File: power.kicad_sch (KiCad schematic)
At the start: 30 parts, among them J1 USB_C_Receptacle_USB2.0_16P, J2 Conn_01x02_MountingPin, Q1 Si2305CDS, Q2 Si2305CDS, Q3 SS8050, SW1 SW_Push, U1 HT7533-1, U2 TP4056-42-ESOP8

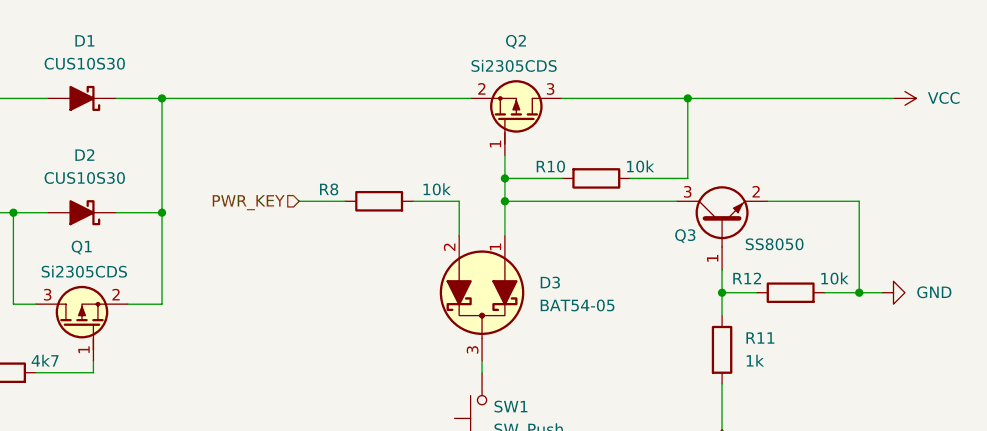
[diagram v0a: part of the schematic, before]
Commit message: 更正电源开关电路的原理错误
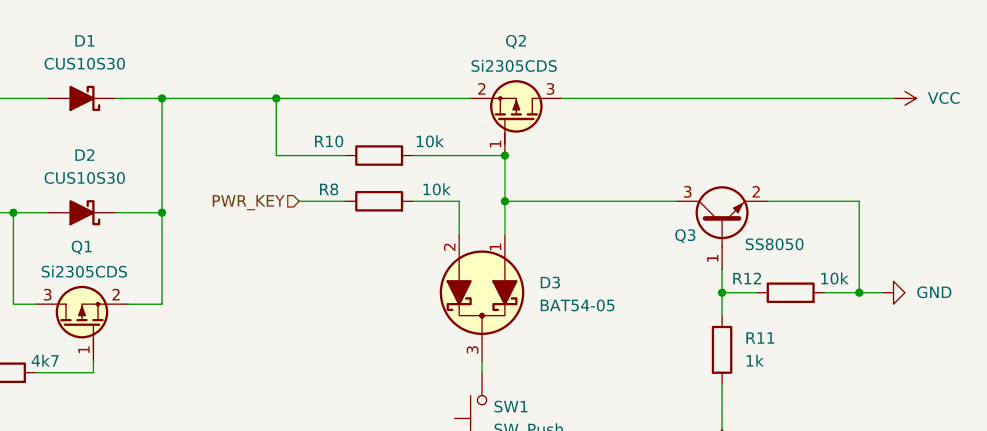
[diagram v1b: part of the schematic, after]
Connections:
- net VCC: no longer R10.1
- net at D1.1 (K), D2.1 (K), Q1.2 (S)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: now also R10.1
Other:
- moved on the sheet: R10
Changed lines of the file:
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@@
+	)
+	(junction
+		(at 203.2 41.91)
+		(diameter 0)
+		(color 0 0 0 0)
 	)
 	(junction
@@
 	)
 	(junction
-		(at 203.2 44.45)
+		(at 177.8 35.56)
 		(diameter 0)
 		(color 0 0 0 0)
@@
 	(junction
 		(at 50.8 118.11)
-		(diameter 0)
-		(color 0 0 0 0)
-	)
-	(junction
-		(at 223.52 35.56)
 		(diameter 0)
 		(color 0 0 0 0)
@@
 	(wire
 		(pts
+			(xy 177.8 35.56) (xy 199.39 35.56)
+		)
+		(stroke
+			(width 0)
+			(type default)
+		)
+	)
+	(wire
+		(pts
+			(xy 177.8 35.56) (xy 177.8 41.91)
+		)
+		(stroke
+			(width 0)
+			(type default)
+		)
+	)
+	(wire
+		(pts
 			(xy 90.17 55.88) (xy 97.79 55.88)
 		)
@@
 	(wire
 		(pts
-			(xy 165.1 35.56) (xy 199.39 35.56)
+			(xy 165.1 35.56) (xy 177.8 35.56)
 		)
 		(stroke
@@
 	(wire
 		(pts
-			(xy 203.2 44.45) (xy 209.55 44.45)
-		)
-		(stroke
-			(width 0)
-			(type default)
-		)
-	)
-	(wire
-		(pts
 			(xy 95.25 35.56) (xy 95.25 48.26)
 		)
@@
 	(wire
 		(pts
-			(xy 223.52 35.56) (xy 246.38 35.56)
-		)
-		(stroke
-			(width 0)
-			(type default)
-		)
-	)
-	(wire
-		(pts
 			(xy 118.11 55.88) (xy 119.38 55.88)
 		)
@@
 	(wire
 		(pts
-			(xy 217.17 44.45) (xy 223.52 44.45)
-		)
-		(stroke
-			(width 0)
-			(type default)
-		)
-	)
-	(wire
-		(pts
 			(xy 165.1 35.56) (xy 165.1 48.26)
 		)
@@
 	(wire
 		(pts
+			(xy 193.04 41.91) (xy 203.2 41.91)
+		)
+		(stroke
+			(width 0)
+			(type default)
+		)
+	)
+	(wire
+		(pts
 			(xy 148.59 58.42) (xy 148.59 48.26)
 		)
@@
 	(wire
 		(pts
-			(xy 209.55 35.56) (xy 223.52 35.56)
+			(xy 209.55 35.56) (xy 246.38 35.56)
 		)
 		(stroke
@@
 	(wire
 		(pts
-			(xy 203.2 46.99) (xy 203.2 44.45)
+			(xy 203.2 41.91) (xy 203.2 46.99)
 		)
 		(stroke
@@
 	(wire
 		(pts
-			(xy 223.52 44.45) (xy 223.52 35.56)
-		)
-		(stroke
-			(width 0)
-			(type default)
-		)
-	)
-	(wire
-		(pts
 			(xy 81.28 114.3) (xy 100.33 114.3)
 		)
@@
 	(wire
 		(pts
-			(xy 203.2 41.91) (xy 203.2 44.45)
-		)
-		(stroke
-			(width 0)
-			(type default)
-		)
-	)
-	(wire
-		(pts
 			(xy 113.03 114.3) (xy 119.38 114.3)
 		)
@@
 		(pts
 			(xy 128.27 48.26) (xy 148.59 48.26)
+		)
+		(stroke
+			(width 0)
+			(type default)
+		)
+	)
+	(wire
+		(pts
+			(xy 185.42 41.91) (xy 177.8 41.91)
 		)
 		(stroke
@@
 	(symbol
 		(lib_id "Device:R")
-		(at 213.36 44.45 270)
+		(at 189.23 41.91 90)
 		(unit 1)
 		(exclude_from_sim no)
@@
 		(dnp no)
 		(property "Reference" "R10"
-			(at 208.28 43.18 90)
+			(at 183.642 40.386 90)
 			(effects
 				(font
@@
 		)
 		(property "Value" "10k"
-			(at 218.186 43.18 90)
+			(at 194.818 40.386 90)
 			(effects
 				(font
@@
 		)
 		(property "Footprint" "Resistor_SMD:R_0603_1608Metric"
-			(at 213.36 42.672 90)
+			(at 189.23 43.688 90)
 			(effects
 				(font
@@
 		)
 		(property "Datasheet" "~"
-			(at 213.36 44.45 0)
+			(at 189.23 41.91 0)
 			(effects
 				(font
@@
 		)
 		(property "Description" "Resistor"
-			(at 213.36 44.45 0)
-			(effects
-				(font
+			(at 189.23 41.91 0)
+			(effects
+				(font
